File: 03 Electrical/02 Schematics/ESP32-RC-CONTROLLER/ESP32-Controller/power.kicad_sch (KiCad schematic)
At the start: 12 parts, among them J1 USB_C_Receptacle_USB2.0_16P, SW1 SW_Nidec_CAS-120A1, U2 LP5912-3.3DRV, U4 LTC4002ES8-4.2

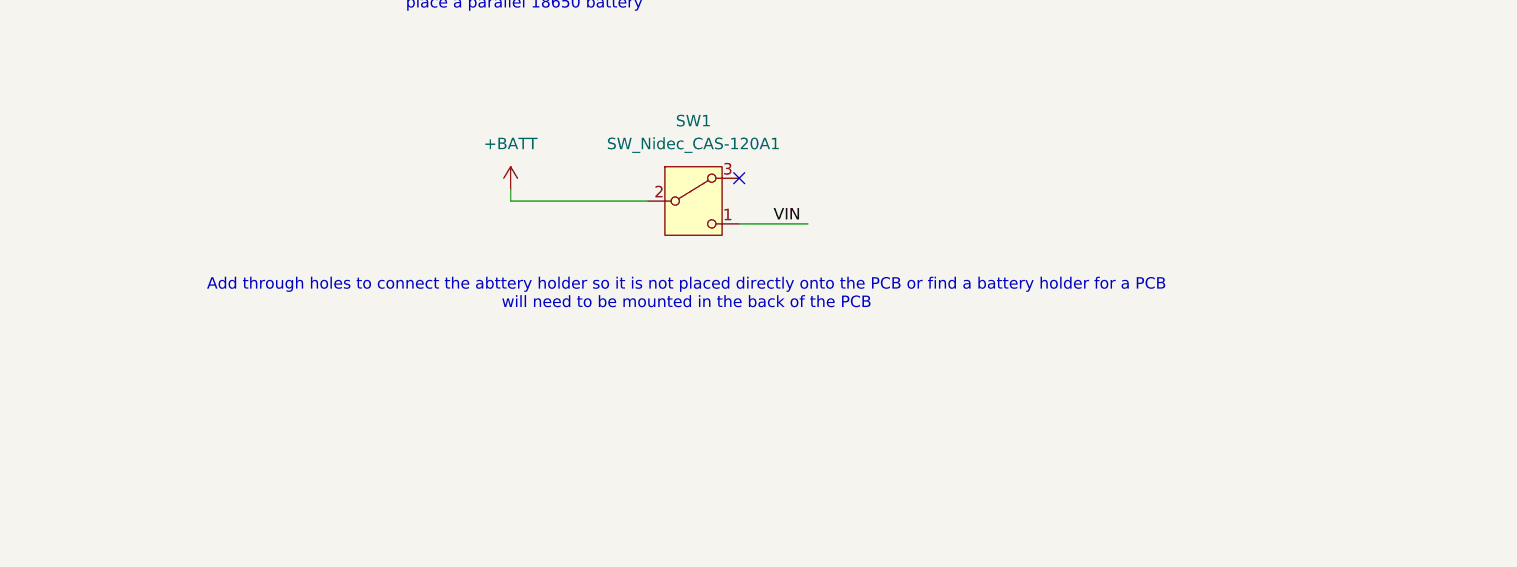
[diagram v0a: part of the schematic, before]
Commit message: added new micro
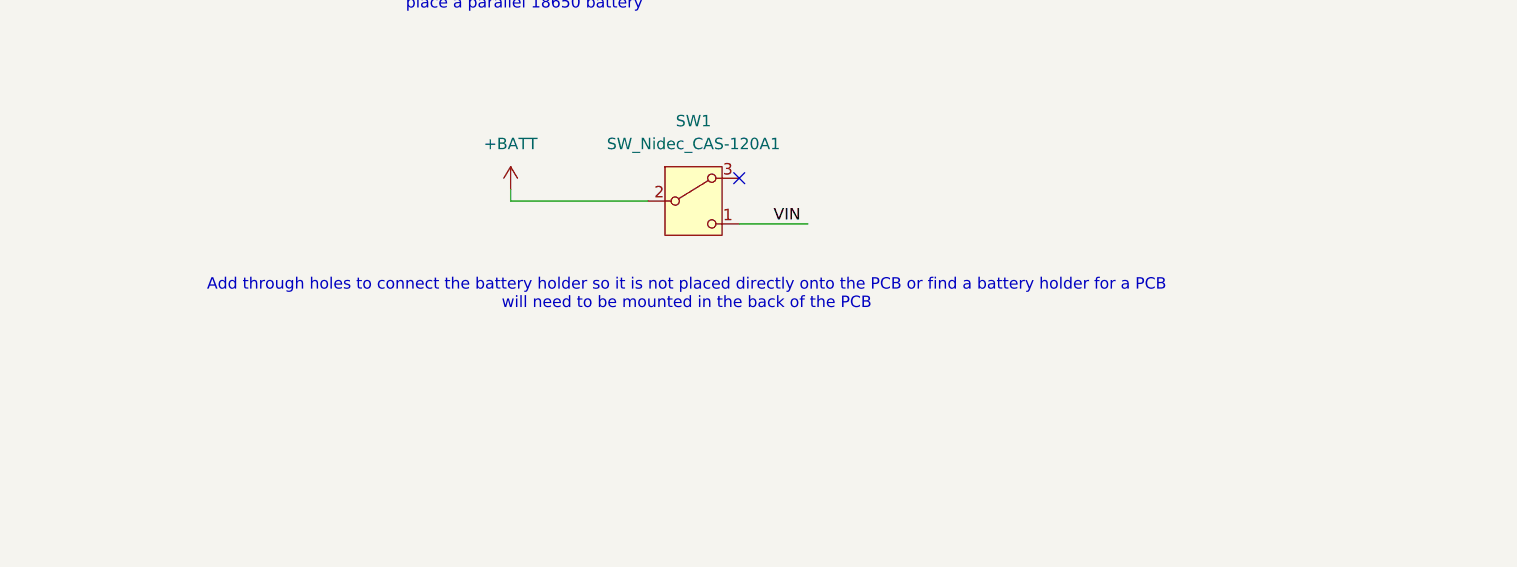
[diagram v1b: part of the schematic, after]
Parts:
- C1: footprint (none) -> Capacitor_SMD:C_0603_1608Metric
- L1: footprint (none) -> Inductor_SMD:L_0603_1608Metric
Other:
- note added: "Add through holes to connect the battery holder so it is not placed directly onto the PCB or find a battery holder for a PCB will need to be mounted in the back of the PCB"
- note removed: "Add through holes to connect the abttery holder so it is not placed directly onto the PCB or find a battery holder for a PCB will need to be mounted in the back of the PCB"
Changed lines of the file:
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@@
 		)
 	)
-	(text "Add through holes to connect the abttery holder so it is not placed directly onto the PCB or find a battery holder for a PCB \nwill need to be mounted in the back of the PCB\n"
+	(text "Add through holes to connect the battery holder so it is not placed directly onto the PCB or find a battery holder for a PCB \nwill need to be mounted in the back of the PCB\n"
 		(exclude_from_sim no)
 		(at 57.658 57.404 0)
@@
 			)
 		)
-		(property "Footprint" ""
+		(property "Footprint" "Inductor_SMD:L_0603_1608Metric"
 			(at 254 92.71 0)
 			(effects
@@
 			)
 		)
-		(property "Footprint" ""
+		(property "Footprint" "Capacitor_SMD:C_0603_1608Metric"
 			(at 246.38 96.52 0)
 			(effects
